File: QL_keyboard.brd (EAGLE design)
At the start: 79.8 x 51.6 mm, 40 parts, among them J1 USB-A-S, J2 AVR_SPI_PRG_6TESTPOINTS, U2 3.3V/150mA, U3 MAX3421ESMD, U4 ATMEGA328P_TQFP, U5 TXB0108PW-TSSOP20, Y1 8MHZ

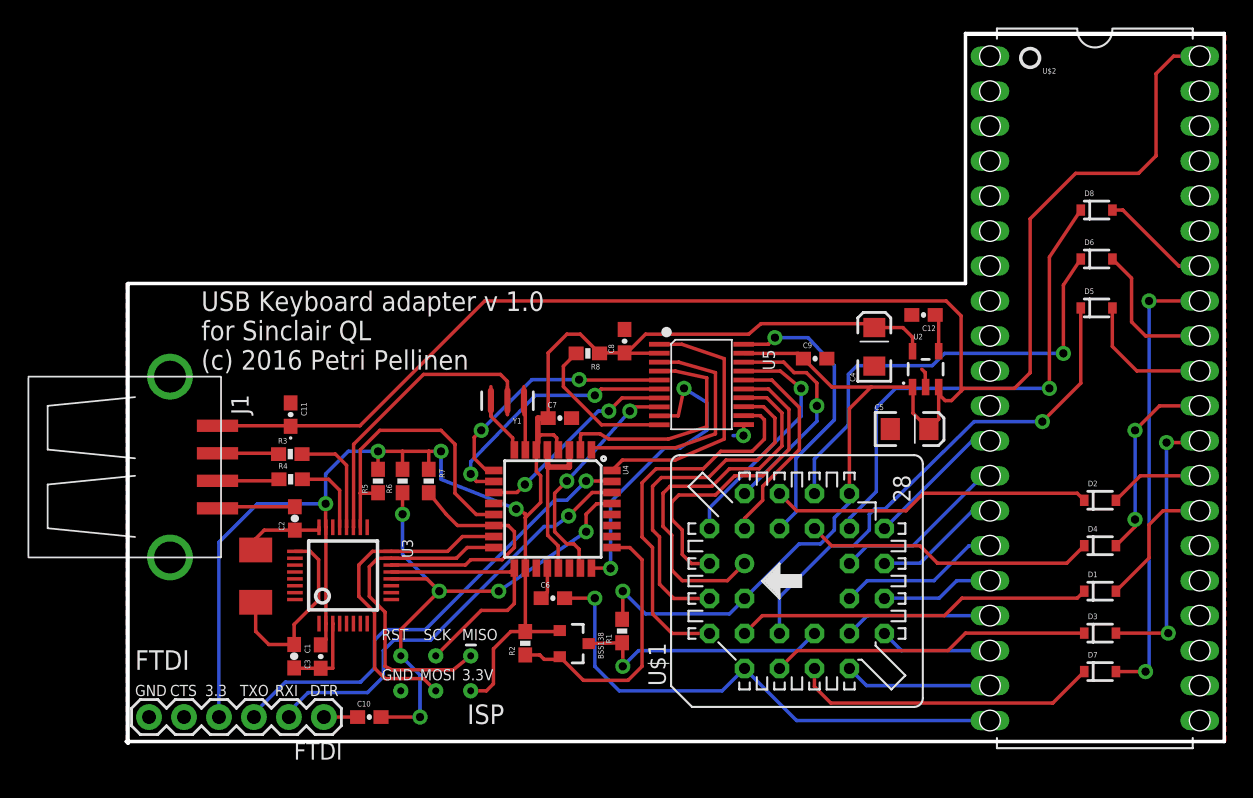
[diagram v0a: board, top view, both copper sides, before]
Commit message: WIP test atmega rotation
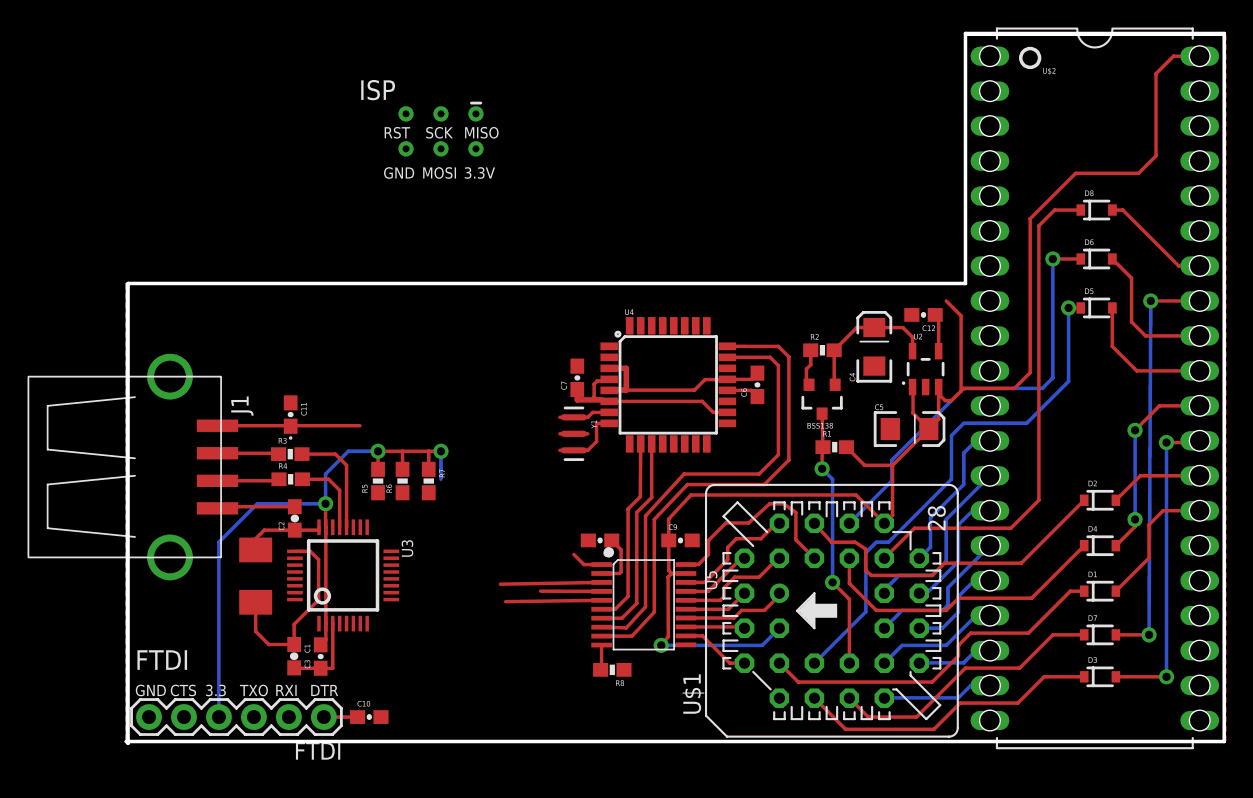
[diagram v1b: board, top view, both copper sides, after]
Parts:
- moved J2 39.4 mm to (22.9, 44.3)
- moved R2 30.3 mm to (50.6, 28.4), turned to 0 degrees
- moved BSS138 25.4 mm to (50.5, 24.9), turned to 180 degrees
- moved R8 23.1 mm to (35.3, 5.21)
- moved C6 21.5 mm to (45.8, 25.9), turned to 90 degrees
- moved R1 20.4 mm to (51.5, 21.4), turned to 0 degrees
- moved U5 16.5 mm to (37.6, 9.93)
- moved C9 16.4 mm to (40.3, 14.6)
- moved C8 14.6 mm to (34.4, 14.6), turned to 180 degrees
- moved U4 12.3 mm to (39.4, 25.9), turned to 0 degrees
- moved Y1 5.40 mm to (32.5, 22.4), turned to 270 degrees
- moved U$1 3.33 mm to (51.3, 9.50)
- moved C7 3.19 mm to (32.8, 26.4), turned to 90 degrees
- moved D3 3.17 mm to (70.7, 4.70)
- moved D7 2.67 mm to (70.7, 7.75)
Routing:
- net GND: track 87.8 -> 26.5 mm, vias 2 -> 0
- net 3.3V: track 122.7 -> 78.3 mm, vias 4 -> 3
- net VCC: track 156.2 -> 113.4 mm
- net RST: track 41.3 -> 0.00 mm, vias 5 -> 0
- net TXO: track 34.5 -> 0.00 mm, vias 1 -> 0
- net RXI: track 31.5 -> 0.00 mm, vias 1 -> 0
- net MISO: track 24.0 -> 0.00 mm
- net MOSI: track 23.8 -> 0.00 mm
- net N$13: track 27.8 -> 5.07 mm
- net INT: track 21.8 -> 0.00 mm
- net N$14: track 26.0 -> 4.29 mm
- net AY2: track 27.7 -> 7.62 mm
- net SCK: track 18.9 -> 0.00 mm
- net AY1: track 23.3 -> 4.73 mm
- net SS: track 18.1 -> 0.00 mm
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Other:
- board text removed: "USB Keyboard adapter v 1.0 for Sinclair QL (c) 2016 Petri Pellinen"

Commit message: WIP second layout version
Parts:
- moved FTDI 38.2 mm to (38.2, 31.6), turned to 0 degrees
- moved C10 34.1 mm to (34.2, 31.6), turned to 180 degrees
- moved C3 21.0 mm to (27.7, 22.1), turned to 180 degrees
- moved C11 20.2 mm to (28.1, 11.6), turned to 90 degrees
- moved XTAL-12MHZ 19.4 mm to (28.1, 17.3), turned to 270 degrees
- moved C1 18.8 mm to (25.3, 19.7)
- moved J2 17.7 mm to (14.1, 29.0), turned to 90 degrees
- moved J1 16.4 mm to (16.3, 10.0)
- moved R4 15.5 mm to (23.7, 9.02)
- moved R3 15.3 mm to (23.7, 11.1)
- moved C6 14.0 mm to (31.9, 24.8), turned to 270 degrees
- moved Y1 14.0 mm to (45.3, 27.9), turned to 90 degrees
- moved C7 13.5 mm to (46.1, 24.3), turned to 270 degrees
- moved U3 13.2 mm to (21.8, 23.7), turned to 180 degrees
- moved C2 13.1 mm to (25.3, 16.4), turned to 270 degrees
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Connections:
- removed net AVR_AX0: U4.32, U5.1
- removed net AVR_AX1: U4.1, U5.3
- removed net AVR_AX2: U4.2, U5.4
- removed net AVR_AY0: U4.9, U5.5
- removed net AVR_AY1: U4.10, U5.6
- removed net AVR_AY2: U4.11, U5.7
- removed net AVR_DATA: U4.24, U5.9
- removed net AVR_STROBE: U4.23, U5.8
- new net N$10: U4.27, U5.6
- new net N$11: U4.28, U5.7
- new net N$12: U4.32, U5.8
- new net N$18: U4.1, U5.9
- new net N$6: U4.23, U5.1
- new net N$7: U4.24, U5.3
- new net N$8: U4.25, U5.4
- new net N$9: U4.26, U5.5
- net RST8808V33: now also U4.2; no longer U4.25
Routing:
- net RST: track 0.00 -> 42.1 mm, vias 0 -> 4
- net AVR_DATA: track 35.2 -> 0.00 mm
- net AVR_STROBE: track 32.5 -> 0.00 mm
- net INT: track 0.00 -> 29.0 mm, vias 0 -> 3
- net N$2: track 8.08 -> 31.8 mm
- net SS: track 0.00 -> 21.6 mm, vias 0 -> 3
- net N$18: track 0.00 -> 20.5 mm
- net MOSI: track 0.00 -> 19.8 mm
- net VCC: track 113.4 -> 131.6 mm
- net N$3: track 5.73 -> 23.9 mm
- net N$12: track 0.00 -> 17.3 mm
- net MISO: track 0.00 -> 16.8 mm
- net AVR_AY2: track 15.0 -> 0.00 mm
- net N$11: track 0.00 -> 14.4 mm
- net SCK: track 0.00 -> 14.4 mm
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
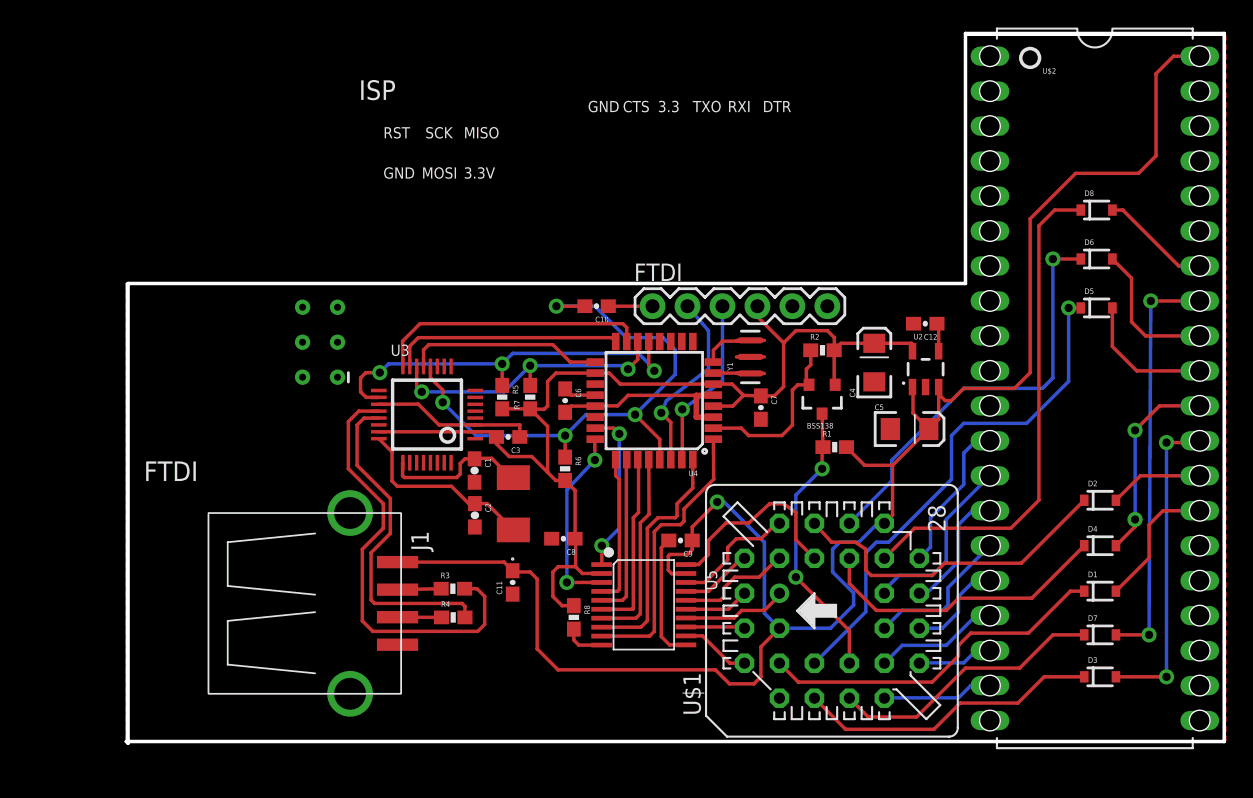
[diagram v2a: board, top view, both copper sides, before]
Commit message: Second, more compact, version of board.
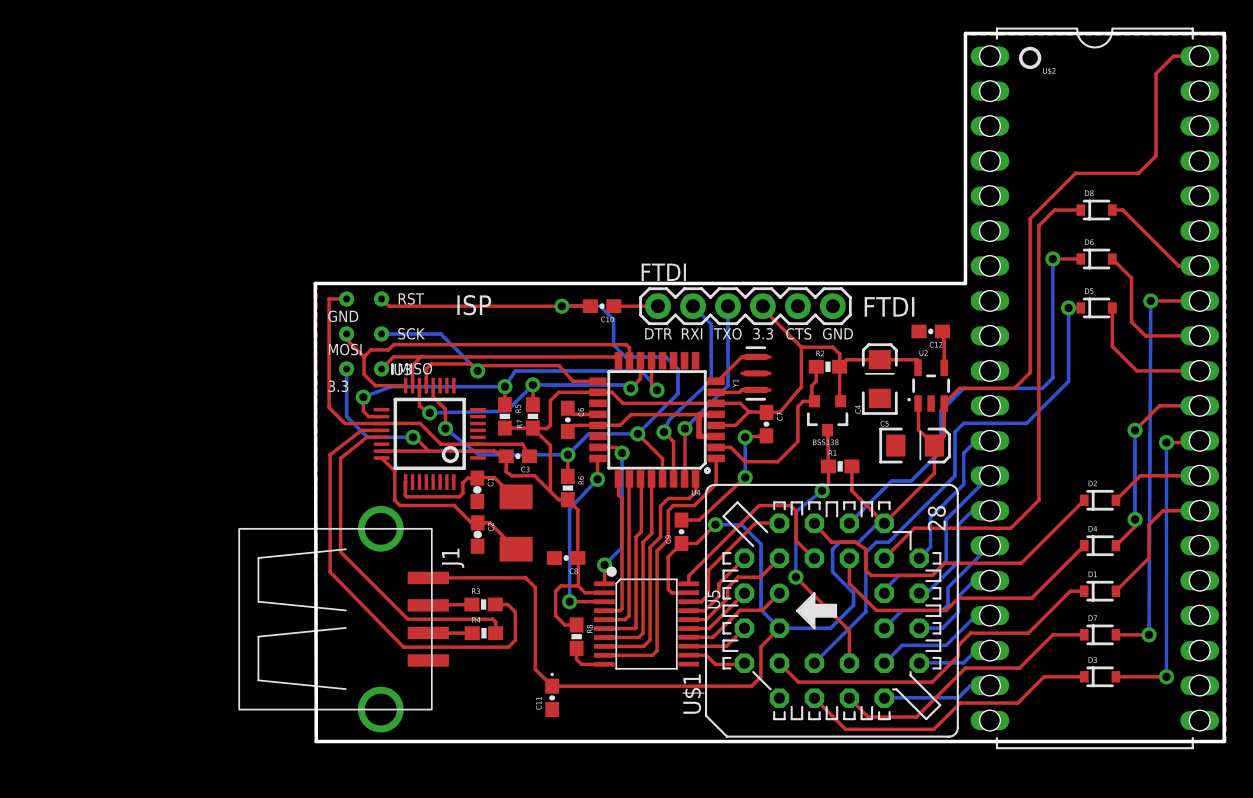
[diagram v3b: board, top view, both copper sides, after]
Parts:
- moved C11 8.86 mm to (30.9, 3.17)
- moved J2 3.26 mm to (17.3, 29.6)
- moved R4 2.51 mm to (26.0, 7.87)
- moved R3 2.51 mm to (26.0, 9.95)
- moved J1 2.51 mm to (18.5, 8.89)
- moved C3 1.57 mm to (28.4, 20.7)
- moved R1 1.46 mm to (51.9, 20.0)
- moved C2 1.41 mm to (25.5, 15.0)
- moved U4 1.41 mm to (38.6, 23.4)
- moved C6 1.41 mm to (32.1, 23.4)
- moved R6 1.41 mm to (32.1, 18.4)
- moved U5 1.41 mm to (37.8, 8.53)
- moved R8 1.41 mm to (32.7, 7.62)
- moved C1 1.41 mm to (25.5, 18.3)
- moved C8 1.41 mm to (31.9, 13.3)
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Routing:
- net RST: track 42.1 -> 57.0 mm
- net GND: track 35.2 -> 49.9 mm, vias 0 -> 2
- net 3.3V: track 81.3 -> 93.1 mm, vias 0 -> 1
- net SCK: track 14.4 -> 22.8 mm, vias 0 -> 1
- net MOSI: track 19.8 -> 27.5 mm
- net MISO: track 16.8 -> 20.0 mm
- net VCC: track 131.6 -> 128.7 mm
- net N$15: track 3.85 -> 2.61 mm
- net RXI: track 13.6 -> 14.8 mm
- net TXO: track 12.7 -> 13.9 mm
- net AX1: track 9.09 -> 10.0 mm
- net AX2: track 5.25 -> 6.16 mm
- net RST8808V5: track 20.6 -> 19.7 mm
- net N$24: track 30.7 -> 31.5 mm
- net N$2: track 31.8 -> 32.6 mm
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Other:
- board size 79.8 x 51.6 mm -> 66 x 51.4 mm
- board text removed: "3.3V"
